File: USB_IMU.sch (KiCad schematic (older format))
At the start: 3 parts, among them U1301 LSM9DS1

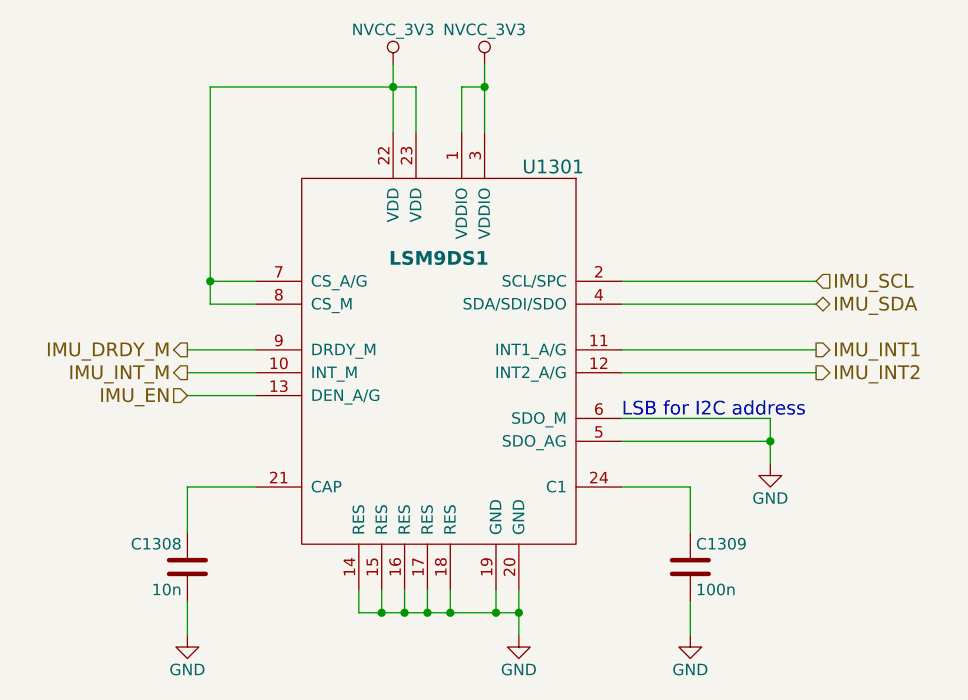
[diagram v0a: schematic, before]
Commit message: Placed a lot of components and routed the audio codec
The BGA of tha audio chipset is to small for regualr technology.
We do not use all of the pins of the chip so we ignore the other
pads and escape throug the balls of the other pad.
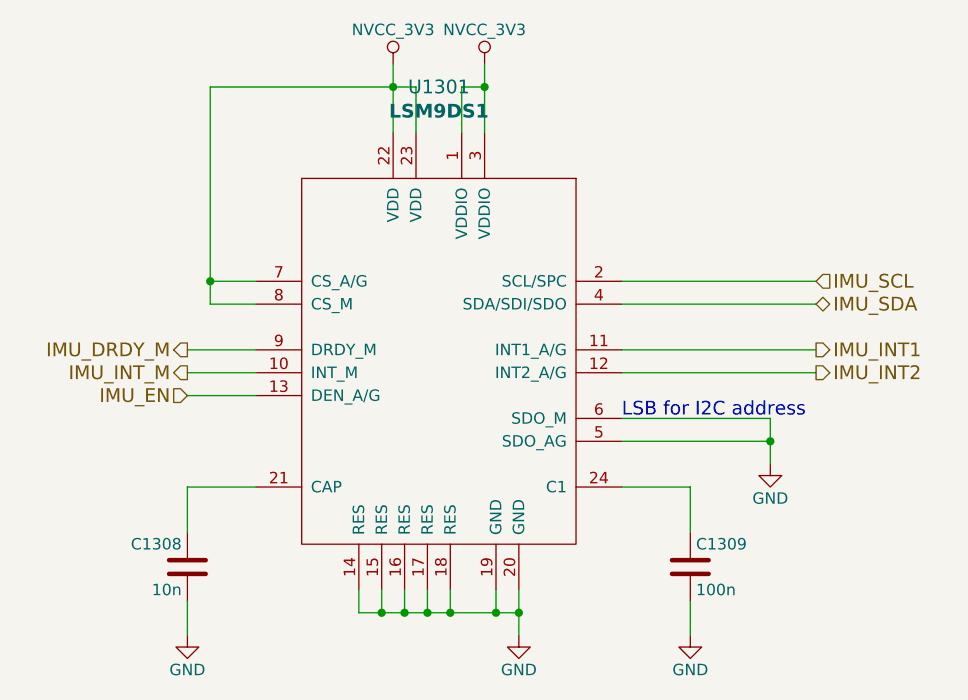
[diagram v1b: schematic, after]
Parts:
- U1301: footprint NokiaRetroFit:LSM9DS1 -> Housings_LGA:LGA-24L_3x3.5mm_Pitch0.43mm
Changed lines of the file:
@@
 LIBS:contrib
 LIBS:valves
-LIBS:tps62742
-LIBS:WM8994ECS
+LIBS:stm32
 LIBS:3210retro-cache
 EELAYER 26 0
@@
 AR Path="/5805F47D/594C5B6F/5942F947" Ref="U1301"  Part="1"
 AR Path="/59B32194/5942F947" Ref="U1301"  Part="1"
-F 0 "U1301" H 6100 5000 60  0000 C CNN
-F 1 "LSM9DS1" H 5600 4600 60  0000 C CNB
-F 2 "NokiaRetroFit:LSM9DS1" H 5600 4000 60  0001 C CNN
+F 0 "U1301" H 5600 5350 60  0000 C CNN
+F 1 "LSM9DS1" H 5600 5244 60  0000 C CNB
+F 2 "Housings_LGA:LGA-24L_3x3.5mm_Pitch0.43mm" H 5600 4000 60  0001 C CNN
 F 3 "" H 5600 4000 60  0001 C CNN
 	1    5600 4000
